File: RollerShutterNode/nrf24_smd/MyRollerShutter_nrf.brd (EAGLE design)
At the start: 47 x 47.9 mm, 53 parts, among them IC1 ATMega-328, IC2 AT25DF512C-SSHN-B, IC3 MCP1703CB, IC4 ACS712_5A, IC5 ATSHA204A, IC6 LM321, U1 MDC3105DMT1, X1 8 MHz

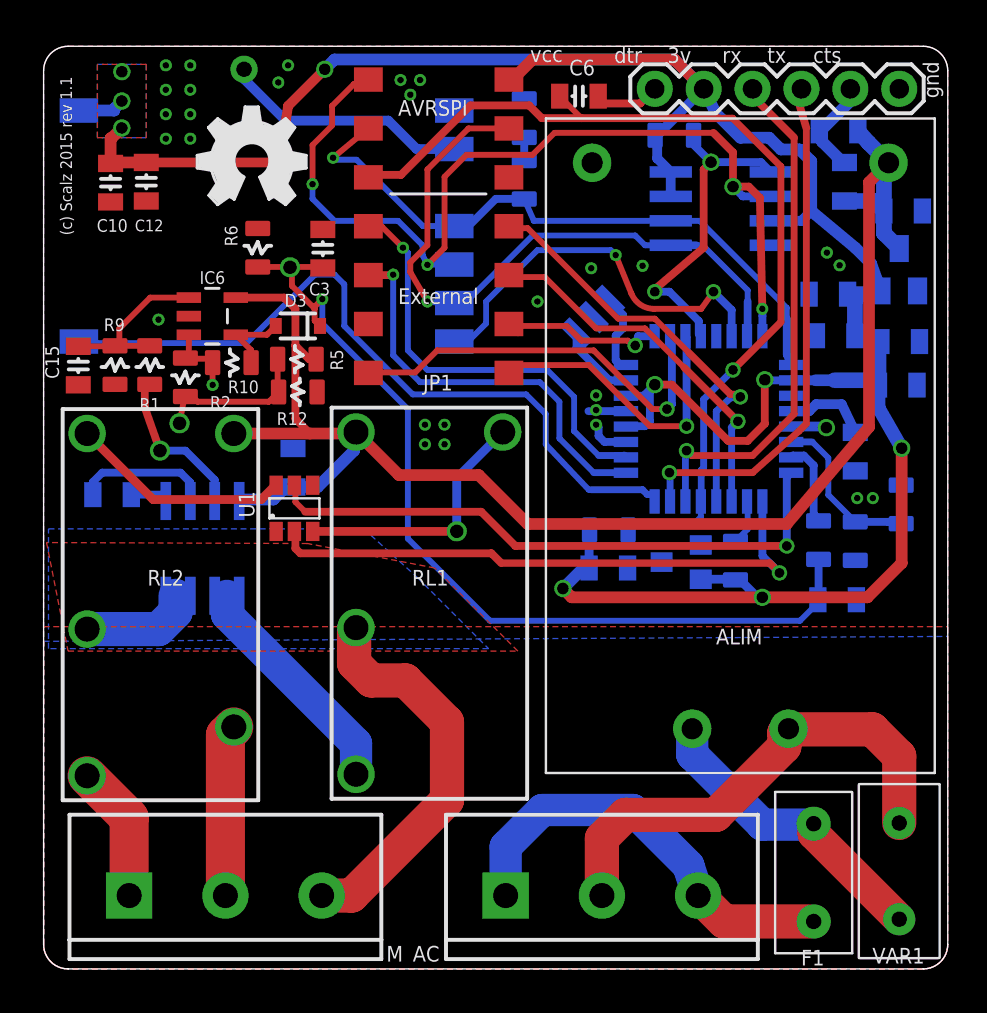
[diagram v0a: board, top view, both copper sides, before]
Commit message: some rerouting and a small fix on connector
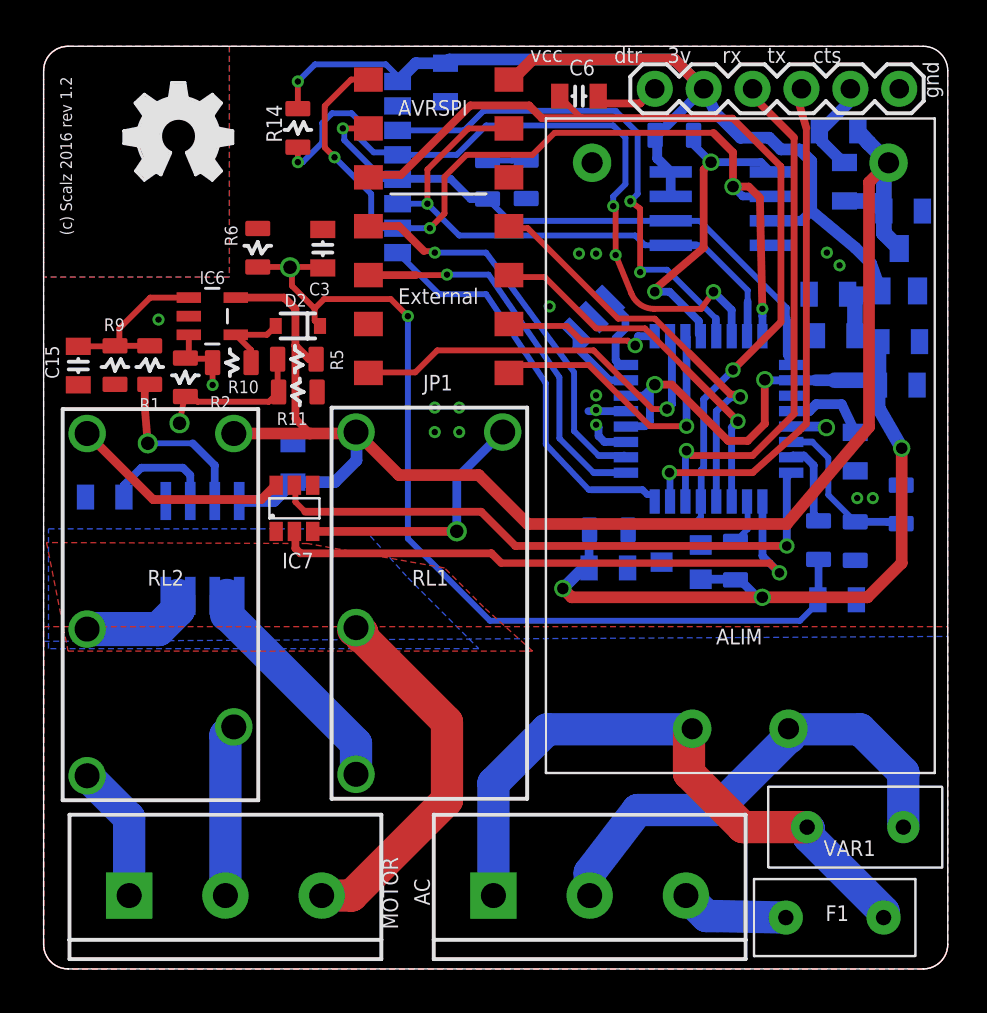
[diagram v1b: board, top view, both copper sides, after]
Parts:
- removed ANT: RFM12B_ANTENNA, LowPowerLab:RFM12B-ANTENNA
- removed C17: 0.1u, LowPowerLab:0805-CAP
- removed D4: LED0805, LowPowerLab:0805-LED
- removed RFM69: RFM69, LowPowerLab:RFM69W-MINPADS
- added D1: LED0805, LowPowerLab:0805-LED
- added NRF_SMD: NRF24L01+SMD_MODULE, pmo_lib:NRF24L01+SMD_MODULE
- added R11: (no value), LowPowerLab:0805-RES
- R12: value (none) -> 1k5
- R14: value 1k5 -> 56k
- moved C12 35.9 mm to (40.8, 35.1), flipped to the bottom, turned to 0 degrees
- moved C10 18.2 mm to (20.9, 46.1), flipped to the bottom
- moved R12 14.8 mm to (23.1, 41.0), flipped to the bottom, turned to 90 degrees
- moved R14 12.1 mm to (13.2, 43.7), flipped to the top
- moved U$4 4.02 mm to (4.17, 41.0)
- moved VAR1 3.23 mm to (42.2, 7.37), turned to 180 degrees
- moved F1 2.58 mm to (41.1, 2.67), turned to 0 degrees
- moved AC 0.64 mm to (23.4, 3.81)
- moved C2 0.40 mm to (3.17, 24.5), turned to 0 degrees
- moved C1 0.25 mm to (13.0, 26.3)
- renumbered D3 to D2, M to MOTOR, R21 to R13, U1 to IC7
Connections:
- net COM renamed OUT_ACS
- net NEUTRE renamed N
- net TOGGLE renamed IN_ACS
- removed net N$4: ANT.P$1, RFM69.ANA
- net D2: now also NRF_SMD.IRQ; no longer RFM69.DIO0
- net D9: now also NRF_SMD.CE
- net GND: now also C12.2, D1.MINUS, NRF_SMD.GND, R11.1; no longer C12.1, C17.2, D4.MINUS, R12.1, RFM69.GND
- net L: no longer AC.1
- net MISO: now also NRF_SMD.MISO; no longer RFM69.MISO
- net MOSI: now also NRF_SMD.MOSI; no longer RFM69.MOSI
- net N$17: now also D1.PLUS, R12.2; no longer D4.PLUS, R14.2
- net N$18: now also R11.2; no longer R12.2
- net PHASE: now also AC.1
- net RF_CSN: now also NRF_SMD.CSN, R14.1; no longer RFM69.NSS
- net SCK: now also NRF_SMD.SCK, R12.1; no longer R14.1, RFM69.SCK
- net VCC: now also C12.1, NRF_SMD.3V, R14.2; no longer C12.2, C17.1, RFM69.VDD
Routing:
- net D9: track 0.03 -> 27.0 mm, vias 0 -> 2
- net PHASE: track 16.0 -> 33.4 mm
- net D2: track 38.7 -> 21.5 mm
- net RF_CSN: track 21.0 -> 38.0 mm, vias 2 -> 4
- net L: track 22.2 -> 5.63 mm
- net VCC: track 142.0 -> 127.0 mm, vias 9 -> 6
- net N$4: track 12.9 -> 0.00 mm
- net MISO: track 51.0 -> 45.0 mm
- net MOSI: track 34.3 -> 29.3 mm
- net GND: track 13.3 -> 11.2 mm, vias 29 -> 16
- net A0: track 47.8 -> 49.8 mm
- net SCK: track 33.7 -> 31.7 mm
- net D4: track 22.4 -> 20.7 mm
- net D3: track 21.4 -> 20.1 mm
- net N$1: track 7.09 -> 5.94 mm
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- added copper zone on layer 1, net N$14
- added copper zone on layer 16, net N$15
- removed copper zone on layer 1, net VCC
- removed copper zone on layer 16, net VCC
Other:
- board text added: "(c) Scalz 2016 rev 1.2"
- board text removed: "(c) Scalz 2015 rev 1.1"
